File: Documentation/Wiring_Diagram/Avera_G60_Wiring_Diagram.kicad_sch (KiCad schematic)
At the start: 15 parts

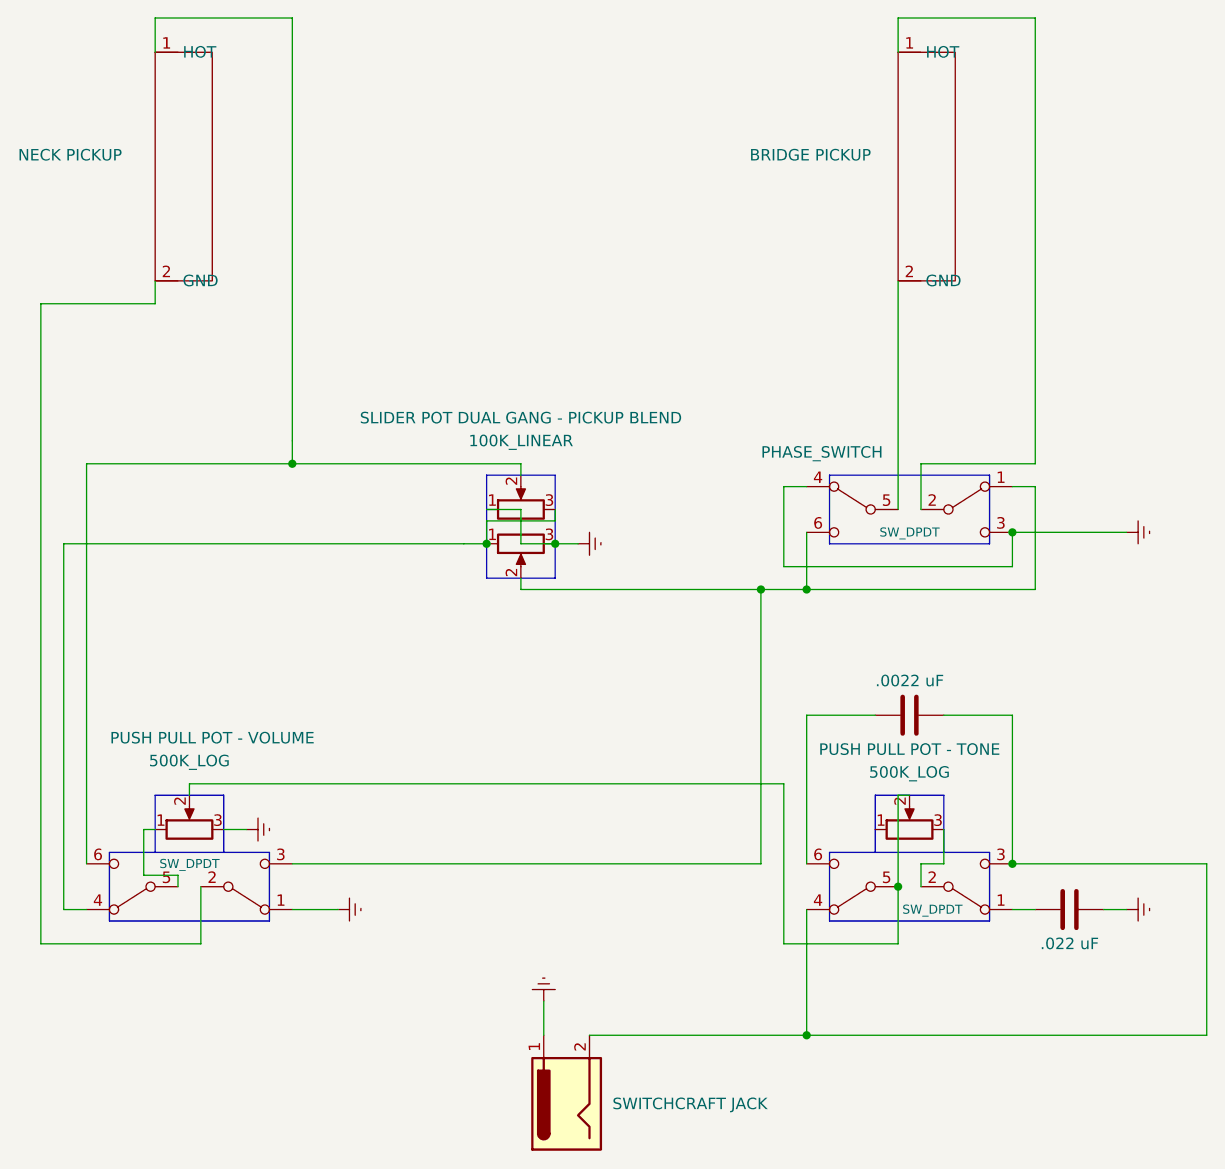
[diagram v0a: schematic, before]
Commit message: update wiring diagram
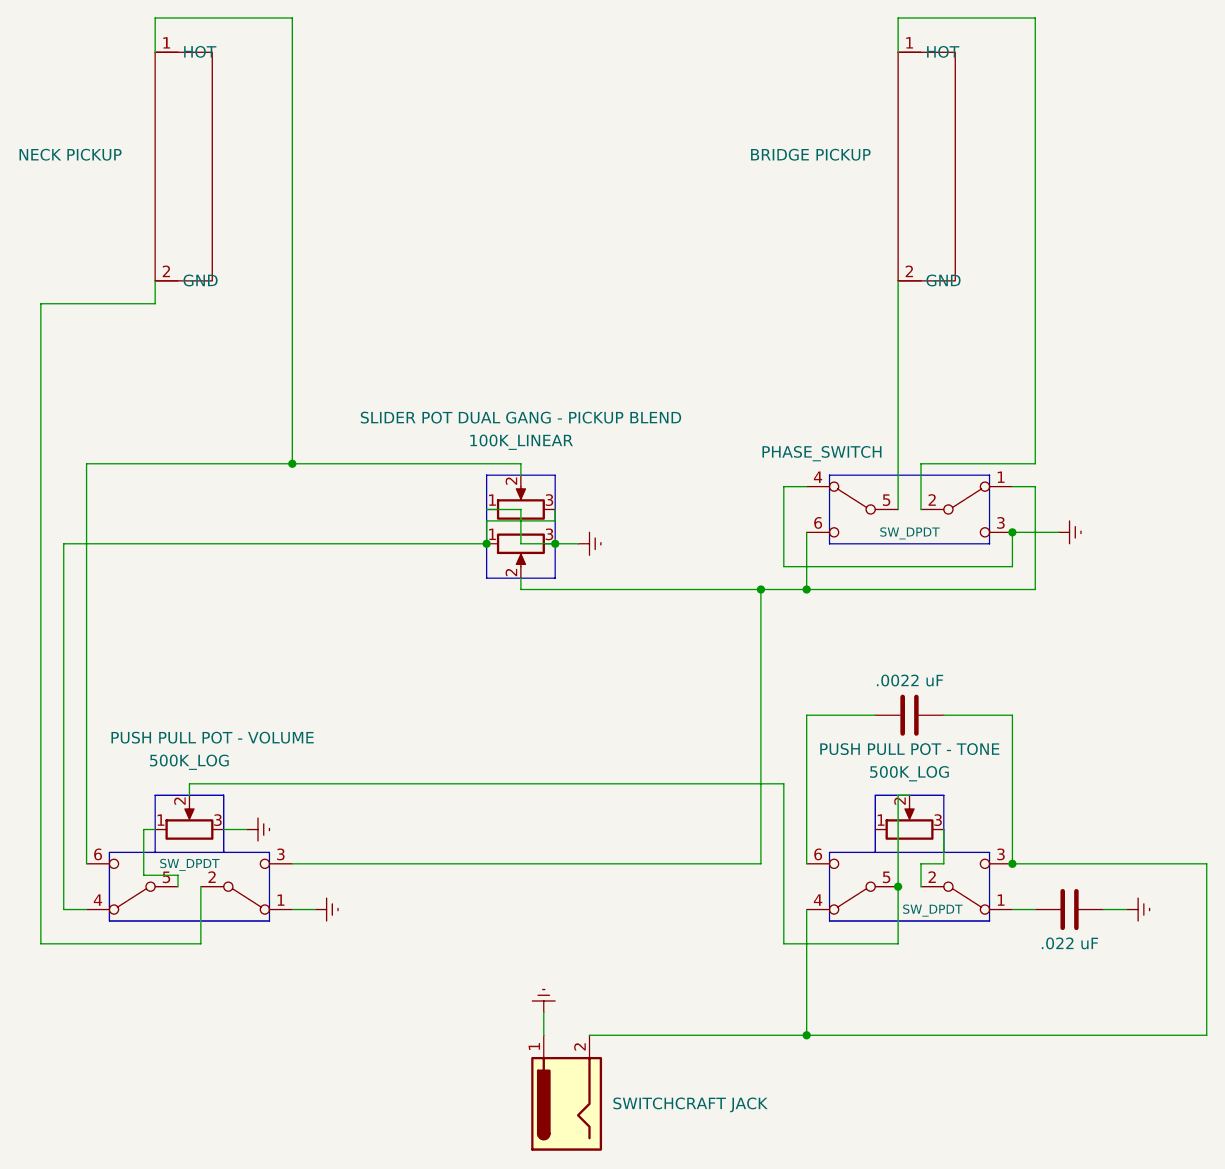
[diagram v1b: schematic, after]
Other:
- company: (none) -> Orion Miller
- title: (none) -> Avera G-60 Wiring Diagram
